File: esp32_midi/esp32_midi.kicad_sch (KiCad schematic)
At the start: 21 parts, among them J2 5V-12V, J3 USB_C_Receptacle_USB2.0, SW1 SW_SPST, U1 ESP32-S3-WROOM-2, U5 AMS1117-5.0, U6 AMS1117-3.3

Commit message: Removed other bullshit projects
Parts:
- gave numbers to parts that had none: 3
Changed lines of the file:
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@@
     (pin "1")
     (instances
-      (project "bobbycar"
-        (path "/477311b9-8f81-40c8-9c55-fd87e287247a"
-          (reference "#PWR?") (unit 1)
-        )
-      )
-      (project "boardcomputer-reinvented"
-        (path "/c34981a4-f5bf-48b8-b827-9a9cfe9c43b8"
-          (reference "#PWR?") (unit 1)
-        )
-      )
       (project "esp32_midi"
         (path "/e33c0603-5c0d-4712-ab63-5756d1504b4c"
@@
     (pin "1")
     (instances
-      (project "bobbycar"
-        (path "/477311b9-8f81-40c8-9c55-fd87e287247a"
-          (reference "#PWR?") (unit 1)
-        )
-      )
-      (project "boardcomputer-reinvented"
-        (path "/c34981a4-f5bf-48b8-b827-9a9cfe9c43b8"
-          (reference "#PWR?") (unit 1)
-        )
-      )
       (project "esp32_midi"
         (path "/e33c0603-5c0d-4712-ab63-5756d1504b4c"
@@
       (project "Smart Home Controller V3"
         (path "/72b36951-3ec7-4569-9c88-cf9b4afe1cae"
-          (reference "#PWR?") (unit 1)
-        )
-      )
-      (project "boardcomputer-reinvented"
-        (path "/c34981a4-f5bf-48b8-b827-9a9cfe9c43b8"
           (reference "#PWR?") (unit 1)
         )
@@
     (pin "6")
     (instances
-      (project "bobbycar"
-        (path "/477311b9-8f81-40c8-9c55-fd87e287247a"
-          (reference "U?") (unit 1)
-        )
-      )
-      (project "boardcomputer-reinvented"
-        (path "/c34981a4-f5bf-48b8-b827-9a9cfe9c43b8"
-          (reference "U?") (unit 1)
-        )
-      )
       (project "esp32_midi"
         (path "/e33c0603-5c0d-4712-ab63-5756d1504b4c"
@@
     (pin "1")
     (instances
-      (project "bobbycar"
-        (path "/477311b9-8f81-40c8-9c55-fd87e287247a"
-          (reference "#PWR?") (unit 1)
-        )
-      )
-      (project "boardcomputer-reinvented"
-        (path "/c34981a4-f5bf-48b8-b827-9a9cfe9c43b8"
-          (reference "#PWR?") (unit 1)
-        )
-      )
       (project "esp32_midi"
         (path "/e33c0603-5c0d-4712-ab63-5756d1504b4c"
@@
         )
       )
-      (project "boardcomputer-reinvented"
-        (path "/c34981a4-f5bf-48b8-b827-9a9cfe9c43b8"
-          (reference "#PWR?") (unit 1)
-        )
-      )
       (project "esp32_midi"
         (path "/e33c0603-5c0d-4712-ab63-5756d1504b4c"
@@
       (project "Smart Home Controller V3"
         (path "/72b36951-3ec7-4569-9c88-cf9b4afe1cae"
-          (reference "C?") (unit 1)
-        )
-      )
-      (project "boardcomputer-reinvented"
-        (path "/c34981a4-f5bf-48b8-b827-9a9cfe9c43b8"
           (reference "C?") (unit 1)
         )
@@
     (pin "6")
     (instances
-      (project "bobbycar"
-        (path "/477311b9-8f81-40c8-9c55-fd87e287247a"
-          (reference "U?") (unit 1)
-        )
-      )
-      (project "boardcomputer-reinvented"
-        (path "/c34981a4-f5bf-48b8-b827-9a9cfe9c43b8"
-          (reference "U?") (unit 1)
-        )
-      )
       (project "esp32_midi"
         (path "/e33c0603-5c0d-4712-ab63-5756d1504b4c"
@@
     (pin "1")
     (instances
-      (project "bobbycar"
-        (path "/477311b9-8f81-40c8-9c55-fd87e287247a"
-          (reference "#PWR?") (unit 1)
-        )
-      )
-      (project "boardcomputer-reinvented"
-        (path "/c34981a4-f5bf-48b8-b827-9a9cfe9c43b8"
-          (reference "#PWR?") (unit 1)
-        )
-      )
       (project "esp32_midi"
         (path "/e33c0603-5c0d-4712-ab63-5756d1504b4c"
@@
     (pin "1")
     (instances
-      (project "bobbycar"
-        (path "/477311b9-8f81-40c8-9c55-fd87e287247a"
-          (reference "#PWR?") (unit 1)
-        )
-      )
-      (project "boardcomputer-reinvented"
-        (path "/c34981a4-f5bf-48b8-b827-9a9cfe9c43b8"
-          (reference "#PWR?") (unit 1)
-        )
-      )
       (project "esp32_midi"
         (path "/e33c0603-5c0d-4712-ab63-5756d1504b4c"
@@
     (pin "6")
     (instances
-      (project "bobbycar"
-        (path "/477311b9-8f81-40c8-9c55-fd87e287247a"
-          (reference "U?") (unit 1)
-        )
-      )
-      (project "boardcomputer-reinvented"
-        (path "/c34981a4-f5bf-48b8-b827-9a9cfe9c43b8"
-          (reference "U?") (unit 1)
-        )
-      )
       (project "esp32_midi"
         (path "/e33c0603-5c0d-4712-ab63-5756d1504b4c"
@@
     (pin "1")
     (instances
-      (project "bobbycar"
-        (path "/477311b9-8f81-40c8-9c55-fd87e287247a"
-          (reference "#PWR?") (unit 1)
-        )
-      )
-      (project "boardcomputer-reinvented"
-        (path "/c34981a4-f5bf-48b8-b827-9a9cfe9c43b8"
-          (reference "#PWR?") (unit 1)
-        )
-      )
       (project "esp32_midi"
         (path "/e33c0603-5c0d-4712-ab63-5756d1504b4c"
@@
     (pin "1")
     (instances
-      (project "bobbycar"
-        (path "/477311b9-8f81-40c8-9c55-fd87e287247a"
-          (reference "#PWR?") (unit 1)
-        )
-      )
-      (project "boardcomputer-reinvented"
-        (path "/c34981a4-f5bf-48b8-b827-9a9cfe9c43b8"
-          (reference "#PWR?") (unit 1)
-        )
-      )
       (project "esp32_midi"
         (path "/e33c0603-5c0d-4712-ab63-5756d1504b4c"
@@
       (project "Smart Home Controller V3"
         (path "/72b36951-3ec7-4569-9c88-cf9b4afe1cae"
-          (reference "#PWR?") (unit 1)
-        )
-      )
-      (project "boardcomputer-reinvented"
-        (path "/c34981a4-f5bf-48b8-b827-9a9cfe9c43b8"
           (reference "#PWR?") (unit 1)
         )
@@
           (reference "J?") (unit 1)
         )
-      )
-      (project "boardcomputer-reinvented"
-        (path "/c34981a4-f5bf-48b8-b827-9a9cfe9c43b8"
-          (reference "J?") (unit 1)
-        )

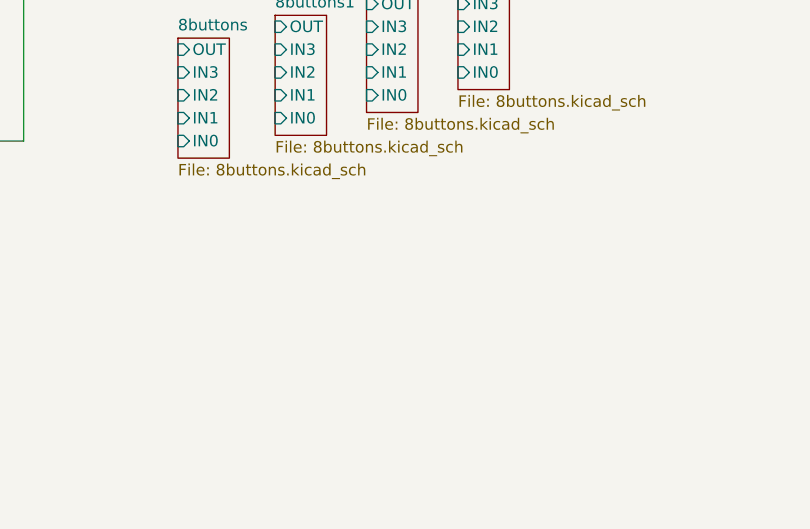
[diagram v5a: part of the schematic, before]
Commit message: Add lights
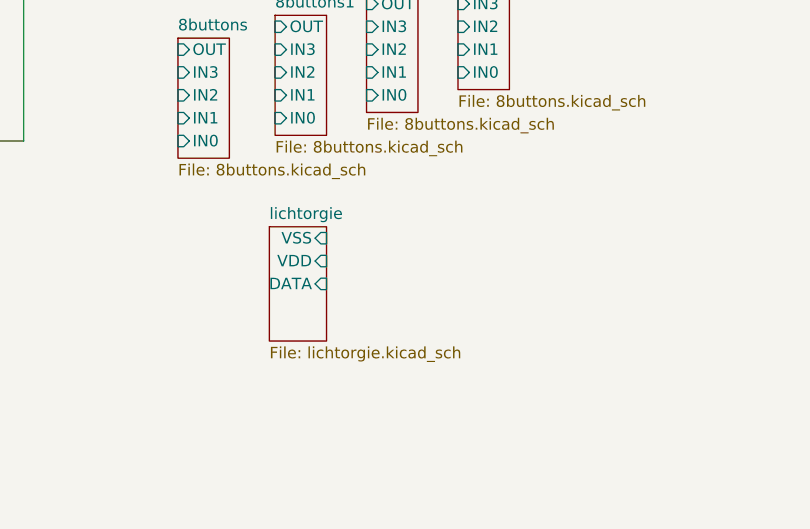
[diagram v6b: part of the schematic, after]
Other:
- added sheet lichtorgie (lichtorgie.kicad_sch)
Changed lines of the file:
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@@
   (symbol (lib_id "power:GND") (at 113.03 19.05 270) (unit 1)
     (in_bom yes) (on_board yes) (dnp no)
-    (property "Reference" "#PWR?" (at 106.68 19.05 0)
+    (property "Reference" "#PWR0103" (at 106.68 19.05 0)
       (effects (font (size 1.27 1.27)) hide)
     )
@@
   (symbol (lib_id "power:GND") (at 213.36 166.37 0) (unit 1)
     (in_bom yes) (on_board yes) (dnp no)
-    (property "Reference" "#PWR?" (at 213.36 172.72 0)
+    (property "Reference" "#PWR0125" (at 213.36 172.72 0)
       (effects (font (size 1.27 1.27)) hide)
     )
@@
   (symbol (lib_id "Power_Protection:USBLC6-4SC6") (at 213.36 156.21 0) (unit 1)
     (in_bom yes) (on_board yes) (dnp no) (fields_autoplaced)
-    (property "Reference" "U?" (at 216.1287 144.6235 0)
+    (property "Reference" "U4" (at 216.1287 144.6235 0)
       (effects (font (size 1.27 1.27)) (justify left))
     )
@@
   (symbol (lib_id "power:GND") (at 95.25 24.13 0) (unit 1)
     (in_bom yes) (on_board yes) (dnp no)
-    (property "Reference" "#PWR?" (at 95.25 30.48 0)
+    (property "Reference" "#PWR0105" (at 95.25 30.48 0)
       (effects (font (size 1.27 1.27)) hide)
     )
@@
   (symbol (lib_id "Power_Protection:USBLC6-4SC6") (at 180.34 156.21 0) (unit 1)
     (in_bom yes) (on_board yes) (dnp no) (fields_autoplaced)
-    (property "Reference" "U?" (at 183.1087 144.6235 0)
+    (property "Reference" "U2" (at 183.1087 144.6235 0)
       (effects (font (size 1.27 1.27)) (justify left))
     )
@@
   (symbol (lib_id "power:GND") (at 198.12 142.24 0) (unit 1)
     (in_bom yes) (on_board yes) (dnp no)
-    (property "Reference" "#PWR?" (at 198.12 148.59 0)
+    (property "Reference" "#PWR0123" (at 198.12 148.59 0)
       (effects (font (size 1.27 1.27)) hide)
     )
@@
   (symbol (lib_id "power:+3V3") (at 198.12 121.92 0) (unit 1)
     (in_bom yes) (on_board yes) (dnp no)
-    (property "Reference" "#PWR?" (at 198.12 125.73 0)
+    (property "Reference" "#PWR0127" (at 198.12 125.73 0)
       (effects (font (size 1.27 1.27)) hide)
     )
@@
   (symbol (lib_id "Power_Protection:USBLC6-4SC6") (at 198.12 132.08 0) (unit 1)
     (in_bom yes) (on_board yes) (dnp no) (fields_autoplaced)
-    (property "Reference" "U?" (at 200.8887 120.4935 0)
+    (property "Reference" "U3" (at 200.8887 120.4935 0)
       (effects (font (size 1.27 1.27)) (justify left))
     )
@@
   (symbol (lib_id "power:+3V3") (at 213.36 146.05 0) (unit 1)
     (in_bom yes) (on_board yes) (dnp no)
-    (property "Reference" "#PWR?" (at 213.36 149.86 0)
+    (property "Reference" "#PWR0124" (at 213.36 149.86 0)
       (effects (font (size 1.27 1.27)) hide)
     )
@@
   (symbol (lib_id "power:GND") (at 180.34 166.37 0) (unit 1)
     (in_bom yes) (on_board yes) (dnp no)
-    (property "Reference" "#PWR?" (at 180.34 172.72 0)
+    (property "Reference" "#PWR0122" (at 180.34 172.72 0)
       (effects (font (size 1.27 1.27)) hide)
     )
@@
       )
     )
+  )
+  (sheet (at 79.375 142.875) (size 6.35 12.7) (fields_autoplaced)
+    (stroke (width 0.1524) (type solid))
+    (fill (color 0 0 0 0.0000))
+    (property "Sheetname" "lichtorgie" (at 79.375 142.1634 0)
+      (effects (font (size 1.27 1.27)) (justify left bottom))
+    )
+    (property "Sheetfile" "lichtorgie.kicad_sch" (at 79.375 156.1596 0)
+      (effects (font (size 1.27 1.27)) (justify left top))
+    )
+    (property "Feld2" "" (at 76.2 146.05 0)
+      (effects (font (size 1.27 1.27)) hide)
+    )
+    (pin "VSS" input (at 85.725 144.145 0)
+      (effects (font (size 1.27 1.27)) (justify right))
+    )
+    (pin "VDD" input (at 85.725 146.685 0)
+      (effects (font (size 1.27 1.27)) (justify right))
+    )
+    (pin "DATA" input (at 85.725 149.225 0)
+      (effects (font (size 1.27 1.27)) (justify right))
+    )
+    (instances
+      (project "esp32_midi"
+        (path "/e33c0603-5c0d-4712-ab63-5756d1504b4c" (page "12"))
+      )
+    )

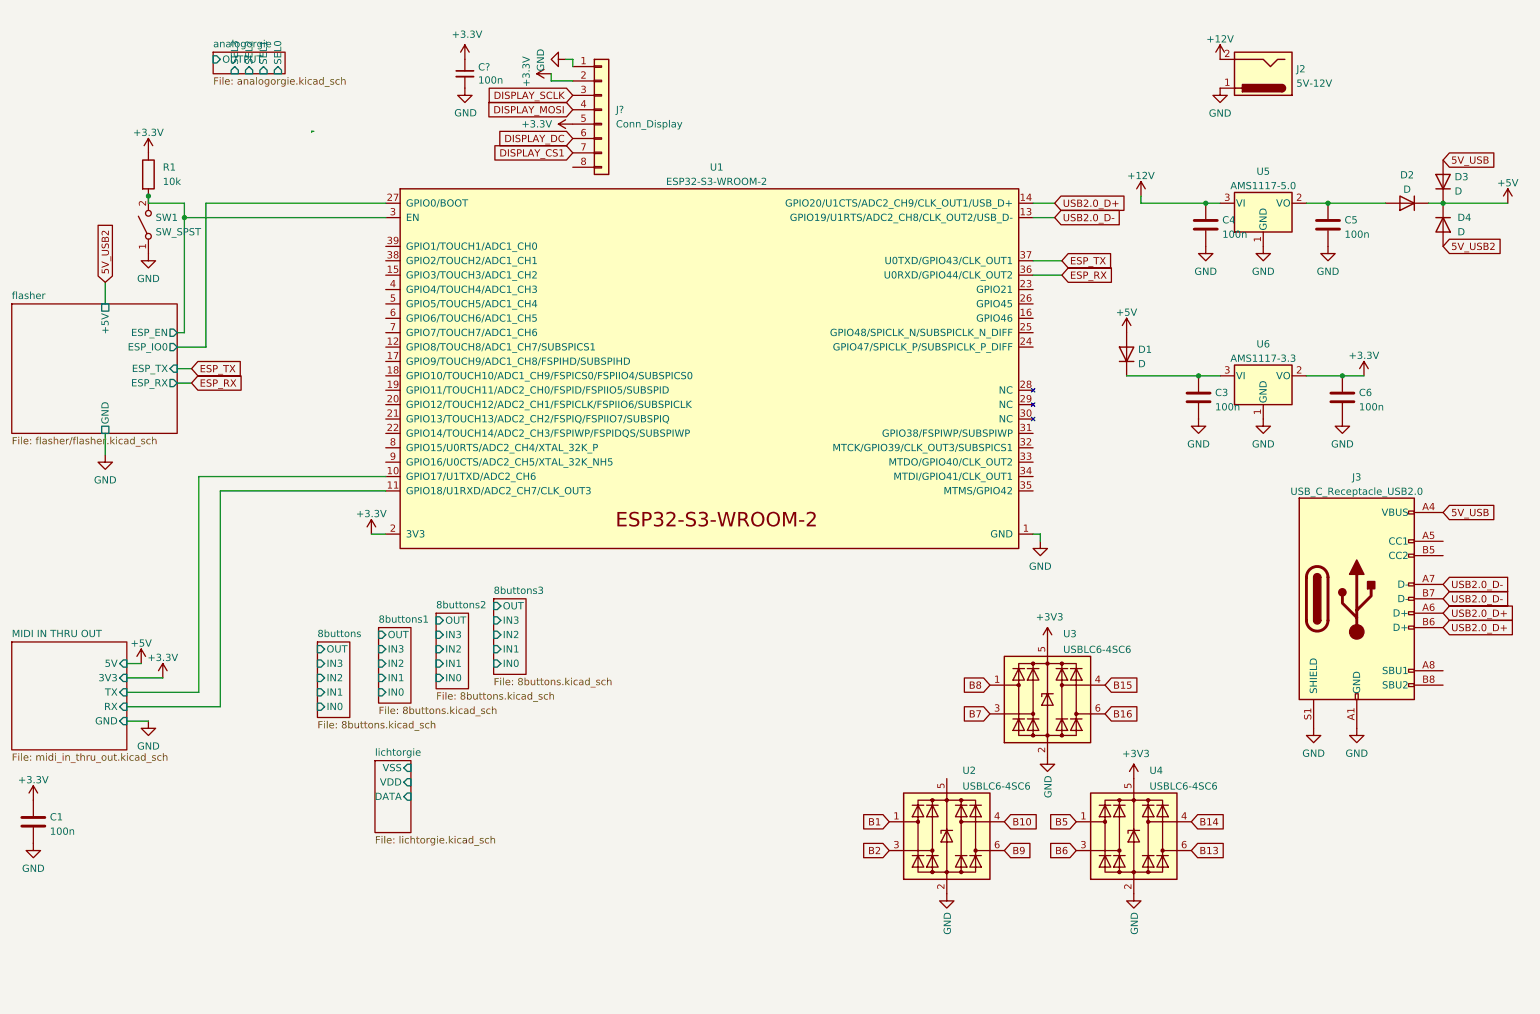
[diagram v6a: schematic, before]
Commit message: Add 64buttons
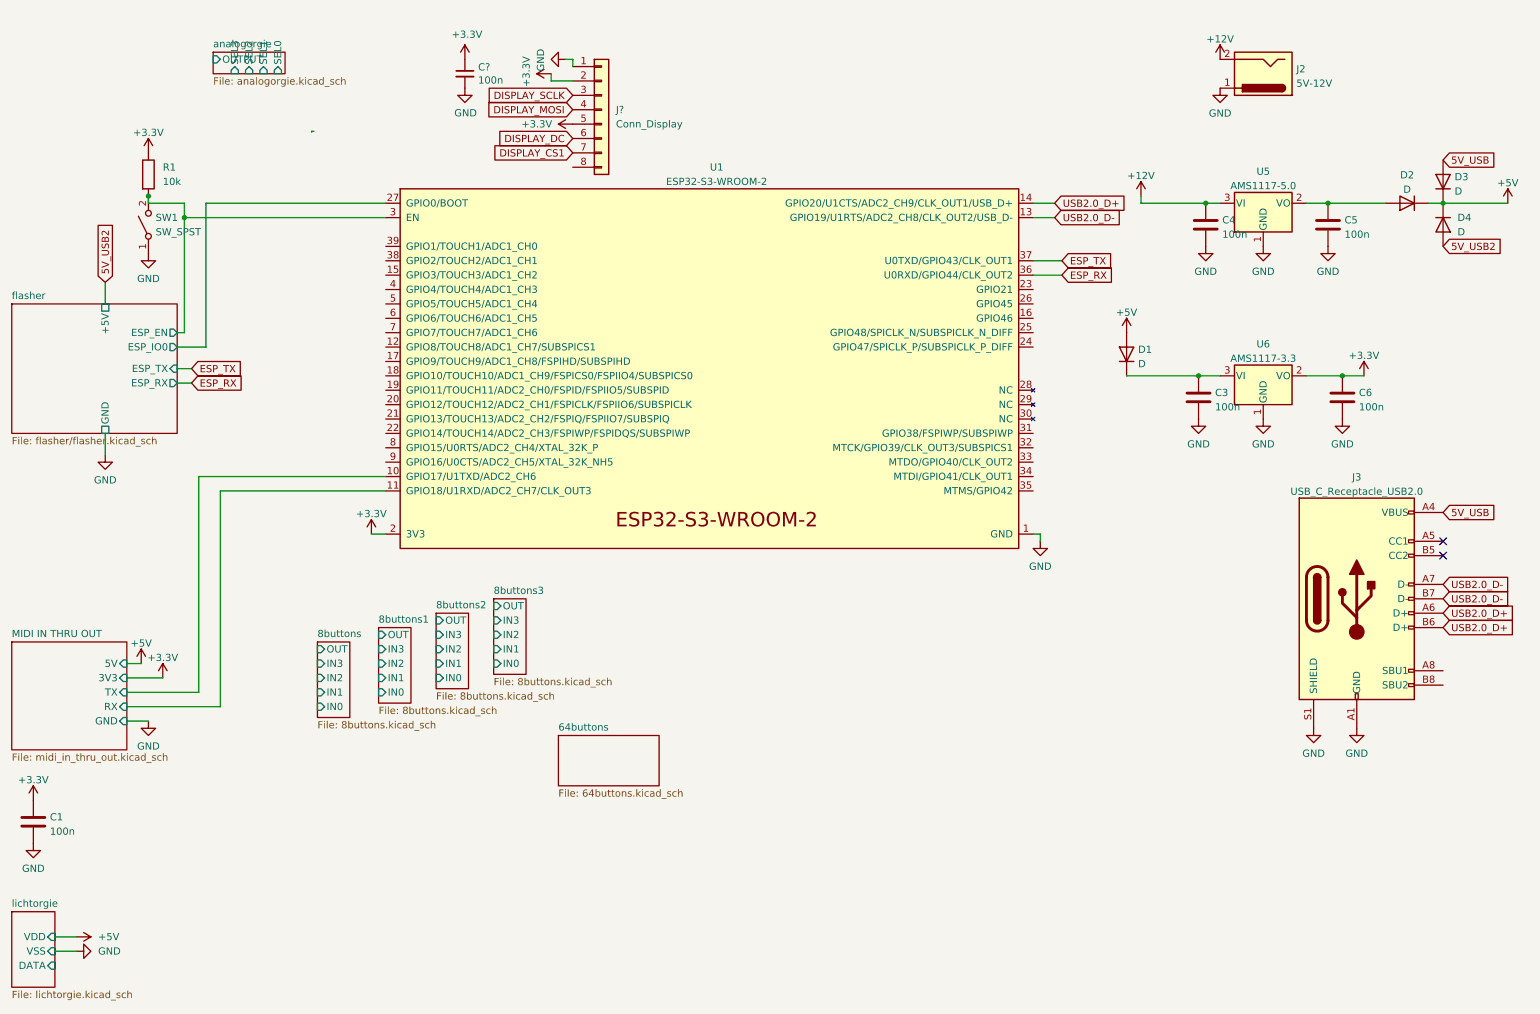
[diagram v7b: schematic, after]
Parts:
- removed U2, U3, U4: USBLC6-4SC6, Package_TO_SOT_SMD:SOT-23-6, symbol Power_Protection:USBLC6-4SC6
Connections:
- no-connect marks 0 -> 2
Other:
- added sheet 64buttons (64buttons.kicad_sch)

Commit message: Updated pcb
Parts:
- renumbered U5 to U2, U6 to U3
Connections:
- net DISPLAY_CS1 is gone; now on net DISPLAY_CS: J?.7 (Pin_7)
- net flasher/ESP_IO0 is gone; now on net flasher/ESP_EN: U1.27 (GPIO0/BOOT)
- net DISPLAY_DC: now also U1.15 (GPIO3/TOUCH3/ADC1_CH2)
- net DISPLAY_MOSI: now also U1.38 (GPIO2/TOUCH2/ADC1_CH1)
- net DISPLAY_SCLK: now also U1.39 (GPIO1/TOUCH1/ADC1_CH0)
- net 64buttons/SEL3: now reaches U1.12 (GPIO8/TOUCH8/ADC1_CH7/SUBSPICS1)
- net 64buttons/SEL4: now reaches U1.17 (GPIO9/TOUCH9/ADC1_CH8/FSPIHD/SUBSPIHD)
- net 64buttons/OUTPUT0: now reaches U1.18 (GPIO10/TOUCH10/ADC1_CH9/FSPICS0/FSPIIO4/SUBSPICS0)
- net 64buttons/OUTPUT1: now reaches U1.19 (GPIO11/TOUCH11/ADC2_CH0/FSPID/FSPIIO5/SUBSPID)
- net analogorgie/OUTPUT0: now reaches U1.20 (GPIO12/TOUCH12/ADC2_CH1/FSPICLK/FSPIIO6/SUBSPICLK)
- net analogorgie/OUTPUT1: now reaches U1.21 (GPIO13/TOUCH13/ADC2_CH2/FSPIQ/FSPIIO7/SUBSPIQ)
- net DISPLAY_CS: now reaches U1.4 (GPIO4/TOUCH4/ADC1_CH3)
- net 64buttons/SEL0: now reaches U1.5 (GPIO5/TOUCH5/ADC1_CH4)
- net 64buttons/SEL1: now reaches U1.6 (GPIO6/TOUCH6/ADC1_CH5)
- net 64buttons/SEL2: now reaches U1.7 (GPIO7/TOUCH7/ADC1_CH6)
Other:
- removed sheet 8buttons
- removed sheet 8buttons1
- removed sheet 8buttons2
- removed sheet 8buttons3
- sheet 64buttons ports: added OUTPUT0, OUTPUT1, SEL0, SEL1, SEL2, SEL3, SEL4; removed none
- sheet analogorgie ports: added OUTPUT0, OUTPUT1; removed OUTPUT
- moved on the sheet: C1, R1, SW1
